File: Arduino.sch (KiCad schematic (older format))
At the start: 0 parts

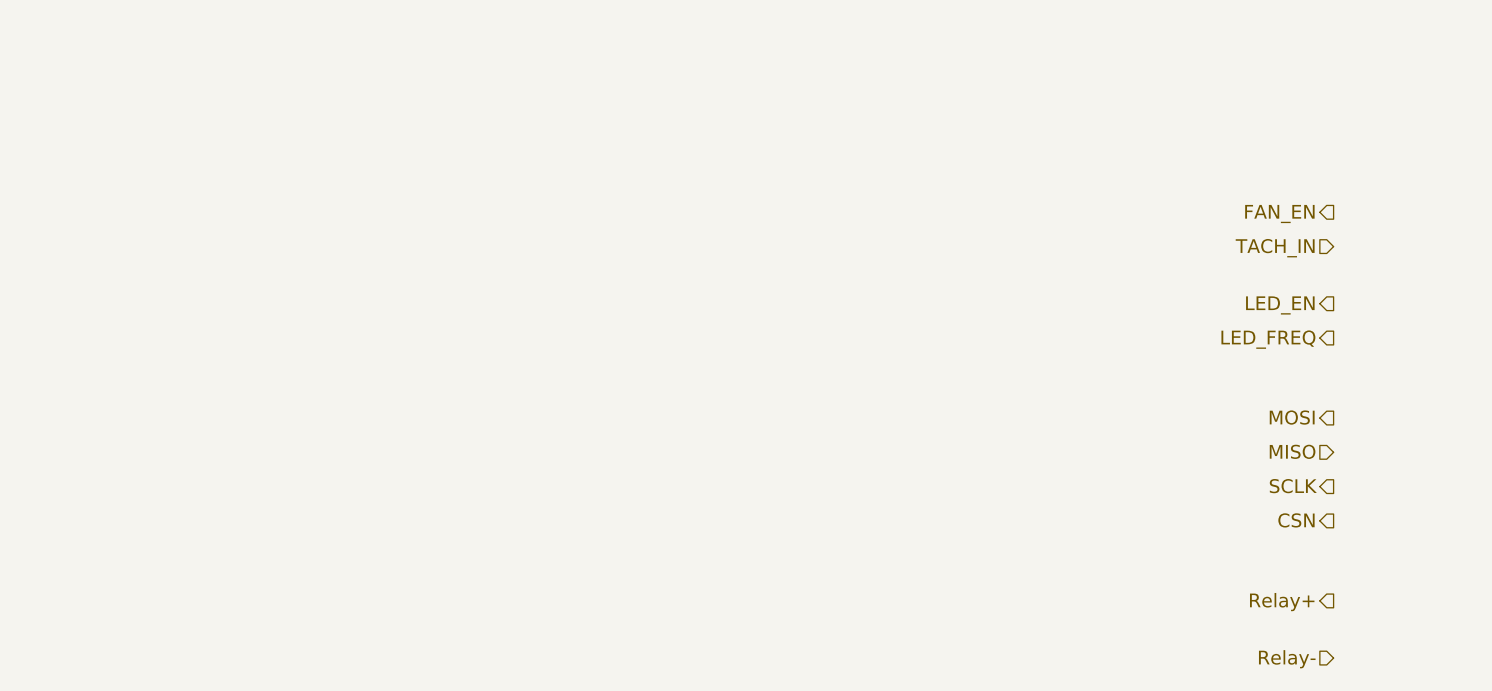
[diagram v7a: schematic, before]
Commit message: WIRED BLOCK DIAGRAM TOGETHER AND ADDED ARDUINO BLOCK
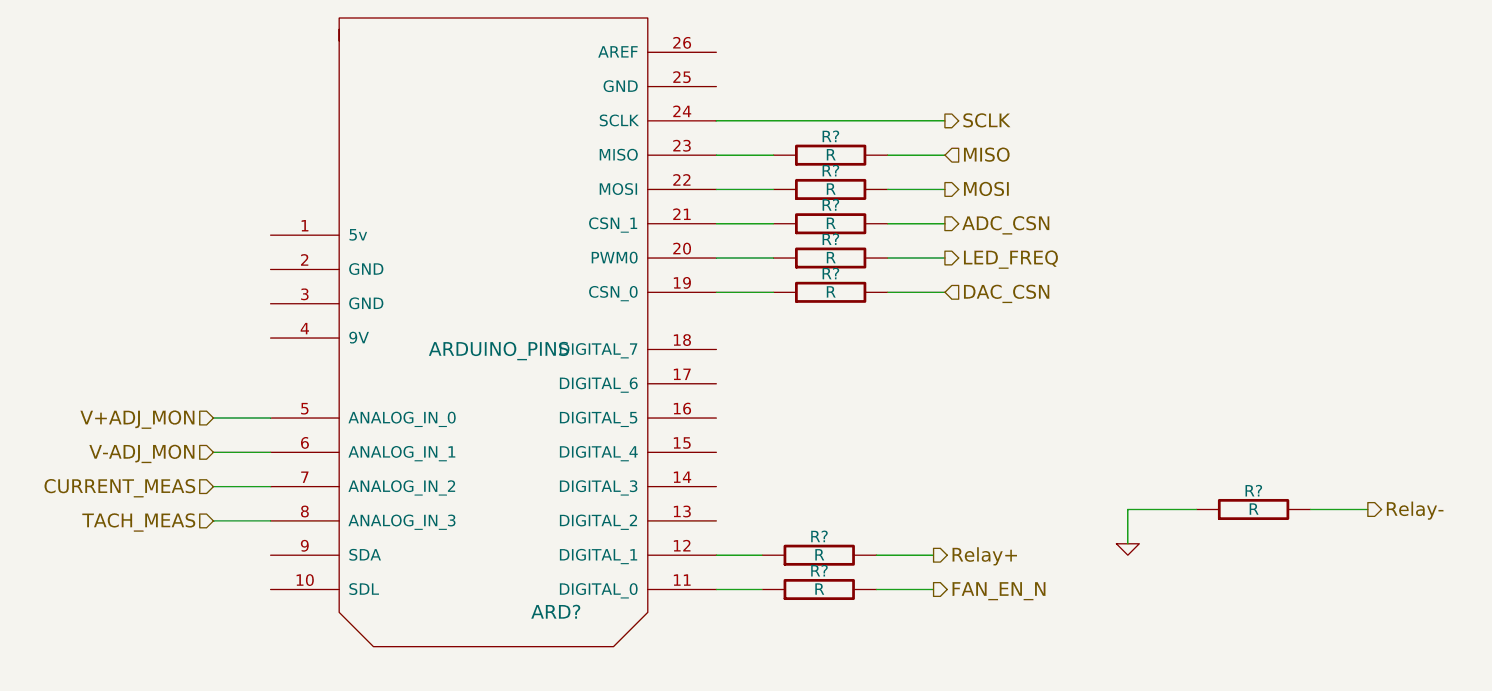
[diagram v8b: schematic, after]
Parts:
- added ARD?: ARDUINO_PINS, symbol ARDUINO_PINS
- added R? (x8): R, symbol R
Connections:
- net LED_FREQ: now also R?.2
- net MISO: now also R?.2
- net MOSI: now also R?.2
- net Relay+: now also R?.2
- net Relay-: now also R?.2
- net SCLK: now also ARD?.24 (SCLK)
- new net: ARD?.11 (DIGITAL_0), R?.1
- new net: ARD?.12 (DIGITAL_1), R?.1
- new net: ARD?.19 (CSN_0), R?.1
- new net: ARD?.20 (PWM0), R?.1
- new net: ARD?.21 (CSN_1), R?.1
- new net: ARD?.22 (MOSI), R?.1
- new net: ARD?.23 (MISO), R?.1
- new net ADC_CSN: R?.2
- new net CURRENT_MEAS: ARD?.7 (ANALOG_IN_2)
- new net DAC_CSN: R?.2
- new net FAN_EN_N: R?.2
- new net GND: R?.1
- new net TACH_MEAS: ARD?.8 (ANALOG_IN_3)
- new net V+ADJ_MON: ARD?.5 (ANALOG_IN_0)
- new net V-ADJ_MON: ARD?.6 (ANALOG_IN_1)
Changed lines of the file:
@@
-EESchema Schematic File Version 2  date Sat 08 Feb 2014 08:25:16 PM EST
+EESchema Schematic File Version 2  date Sat 08 Feb 2014 11:37:49 PM EST
 LIBS:power
 LIBS:device
@@
 $Descr A4 11700 8267
 encoding utf-8
-Sheet 8 9
+Sheet 4 9
 Title ""
 Date "9 feb 2014"
@@
 Comment4 ""
 $EndDescr
-Text HLabel 9700 3550 0    60   Input ~ 0
-TACH_IN
-Text HLabel 9700 3400 0    60   Output ~ 0
-FAN_EN
-Text HLabel 9700 3950 0    60   Output ~ 0
+Wire Wire Line
+	8000 3750 7750 3750
+Wire Wire Line
+	9600 4700 9850 4700
+Wire Wire Line
+	7750 3450 8000 3450
+Wire Wire Line
+	7750 3150 8000 3150
+Wire Wire Line
+	7000 3750 7250 3750
+Wire Wire Line
+	7000 3450 7250 3450
+Wire Wire Line
+	7000 3150 7250 3150
+Wire Wire Line
+	7700 4900 7950 4900
+Wire Wire Line
+	7000 4900 7200 4900
+Wire Wire Line
+	7700 5050 7950 5050
+Wire Wire Line
+	4800 4300 5050 4300
+Wire Wire Line
+	4800 4600 5050 4600
+Wire Wire Line
+	8800 4850 8800 4700
+Wire Wire Line
+	4800 4750 5050 4750
+Wire Wire Line
+	4800 4450 5050 4450
+Wire Wire Line
+	7000 5050 7200 5050
+Wire Wire Line
+	7000 3000 8000 3000
+Wire Wire Line
+	7000 3300 7250 3300
+Wire Wire Line
+	7000 3600 7250 3600
+Wire Wire Line
+	7750 3300 8000 3300
+Wire Wire Line
+	8800 4700 9100 4700
+Wire Wire Line
+	7750 3600 8000 3600
+Text HLabel 8000 3750 2    60   Input ~ 0
+DAC_CSN
+$Comp
+L R R?
+U 1 1 52F700CE
+P 9350 4700
+F 0 "R?" V 9430 4700 50  0000 C CNN
+F 1 "R" V 9350 4700 50  0000 C CNN
+	1    9350 4700
+	0    -1   -1   0
+$EndComp
+Text HLabel 4800 4450 0    60   Input ~ 0
+V-ADJ_MON
+Text HLabel 4800 4300 0    60   Input ~ 0
+V+ADJ_MON
+$Comp
+L R R?
+U 1 1 52F6FBFD
+P 7500 3150
+F 0 "R?" V 7580 3150 50  0000 C CNN
+F 1 "R" V 7500 3150 50  0000 C CNN
+	1    7500 3150
+	0    -1   -1   0
+$EndComp
+$Comp
+L R R?
+U 1 1 52F6FBFA
+P 7500 3300
+F 0 "R?" V 7580 3300 50  0000 C CNN
+F 1 "R" V 7500 3300 50  0000 C CNN
+	1    7500 3300
+	0    -1   -1   0
+$EndComp
+$Comp
+L R R?
+U 1 1 52F6FBF6
+P 7500 3450
+F 0 "R?" V 7580 3450 50  0000 C CNN
+F 1 "R" V 7500 3450 50  0000 C CNN
+	1    7500 3450
+	0    -1   -1   0
+$EndComp
+$Comp
+L R R?
+U 1 1 52F6FBF0
+P 7500 3600
+F 0 "R?" V 7580 3600 50  0000 C CNN
+F 1 "R" V 7500 3600 50  0000 C CNN
+	1    7500 3600
+	0    -1   -1   0
+$EndComp
+$Comp
+L GND #PWR?
+U 1 1 52F6FBAC
+P 8800 4850
+F 0 "#PWR?" H 8800 4850 30  0001 C CNN
+F 1 "GND" H 8800 4780 30  0001 C CNN
+	1    8800 4850
+	1    0    0    -1
+$EndComp
+$Comp
+L R R?
+U 1 1 52F6FB9D
+P 7500 3750
+F 0 "R?" V 7580 3750 50  0000 C CNN
+F 1 "R" V 7500 3750 50  0000 C CNN
+	1    7500 3750
+	0    -1   -1   0
+$EndComp
+$Comp
+L R R?
+U 1 1 52F6FABB
+P 7450 4900
+F 0 "R?" V 7530 4900 50  0000 C CNN
+F 1 "R" V 7450 4900 50  0000 C CNN
+	1    7450 4900
+	0    -1   -1   0
+$EndComp
+$Comp
+L R R?
+U 1 1 52F6FA37
+P 7450 5050
+F 0 "R?" V 7530 5050 50  0000 C CNN
+F 1 "R" V 7450 5050 50  0000 C CNN
+	1    7450 5050
+	0    -1   -1   0
+$EndComp
+Text HLabel 4800 4600 0    60   Input ~ 0
+CURRENT_MEAS
+$Comp
+L ARDUINO_PINS ARD?
+U 1 1 52F6F8AD
+P 6050 3950
+F 0 "ARD?" H 6300 2750 60  0000 C CNN
+F 1 "ARDUINO_PINS" H 6050 3900 60  0000 C CNN
+	1    6050 3950
+	1    0    0    -1
+$EndComp
+Text HLabel 4800 4750 0    60   Input ~ 0
+TACH_MEAS
+Text HLabel 7950 5050 2    60   Output ~ 0
+FAN_EN_N
+Text HLabel 8000 3600 2    60   Output ~ 0
 LED_FREQ
-Text HLabel 9700 3800 0    60   Output ~ 0
-LED_EN
-Text HLabel 9700 4750 0    60   Output ~ 0
-CSN
-Text HLabel 9700 4600 0    60   Output ~ 0
+Text HLabel 8000 3450 2    60   Output ~ 0
+ADC_CSN
+Text HLabel 8000 3000 2    60   Output ~ 0
 SCLK
-Text HLabel 9700 4450 0    60   Input ~ 0
+Text HLabel 8000 3150 2    60   Input ~ 0
 MISO
-Text HLabel 9700 4300 0    60   Output ~ 0
+Text HLabel 8000 3300 2    60   Output ~ 0
 MOSI
-Text HLabel 9700 5350 0    60   Input ~ 0
+Text HLabel 9850 4700 2    60   Output ~ 0
 Relay-
-Text HLabel 9700 5100 0    60   Output ~ 0
+Text HLabel 7950 4900 2    60   Output ~ 0
 Relay+
 $EndSCHEMATC
